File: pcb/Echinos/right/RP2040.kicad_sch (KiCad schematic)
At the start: 28 parts, among them SW224 Button, SW225 Button, SW226 Button, SW227 Button, U200 W25Q128JVP, U201 RP2040, Y200 Crystal_GND24

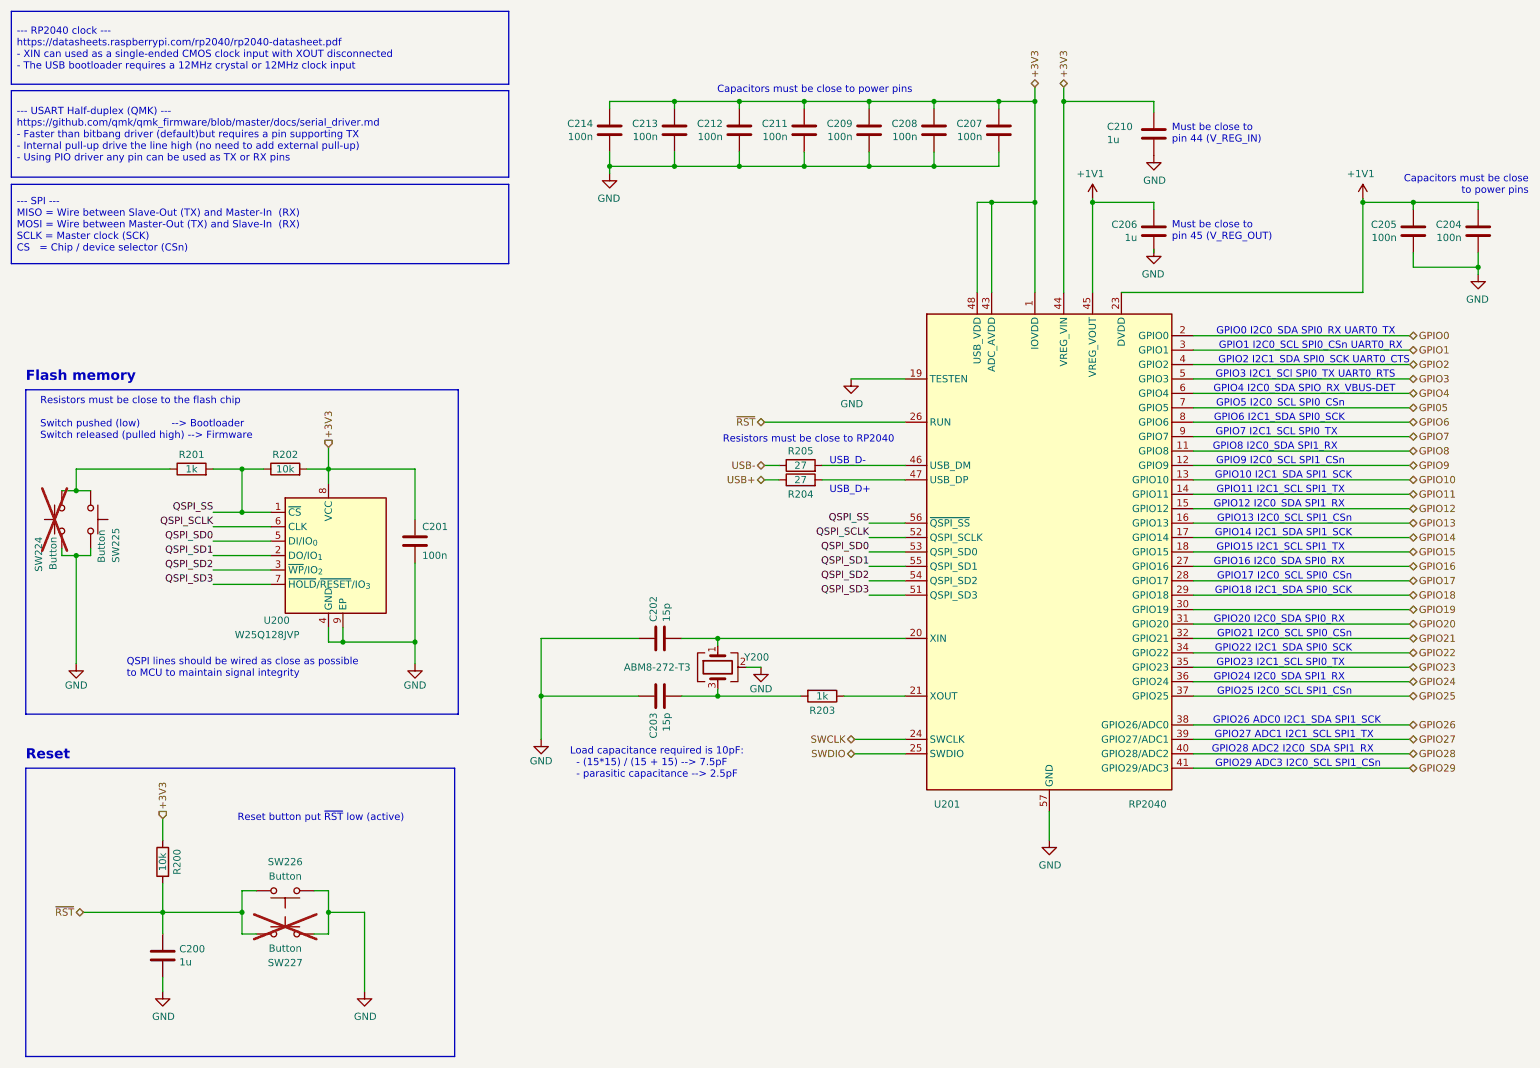
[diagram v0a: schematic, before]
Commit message: 💥 [PCB] - Group left and right on the same PCB.   - Schematics are different for each side   - Split trace naming to avoid mixing right and left   - Add mouse bite between both halves to make manufacturing easier (new footprint)
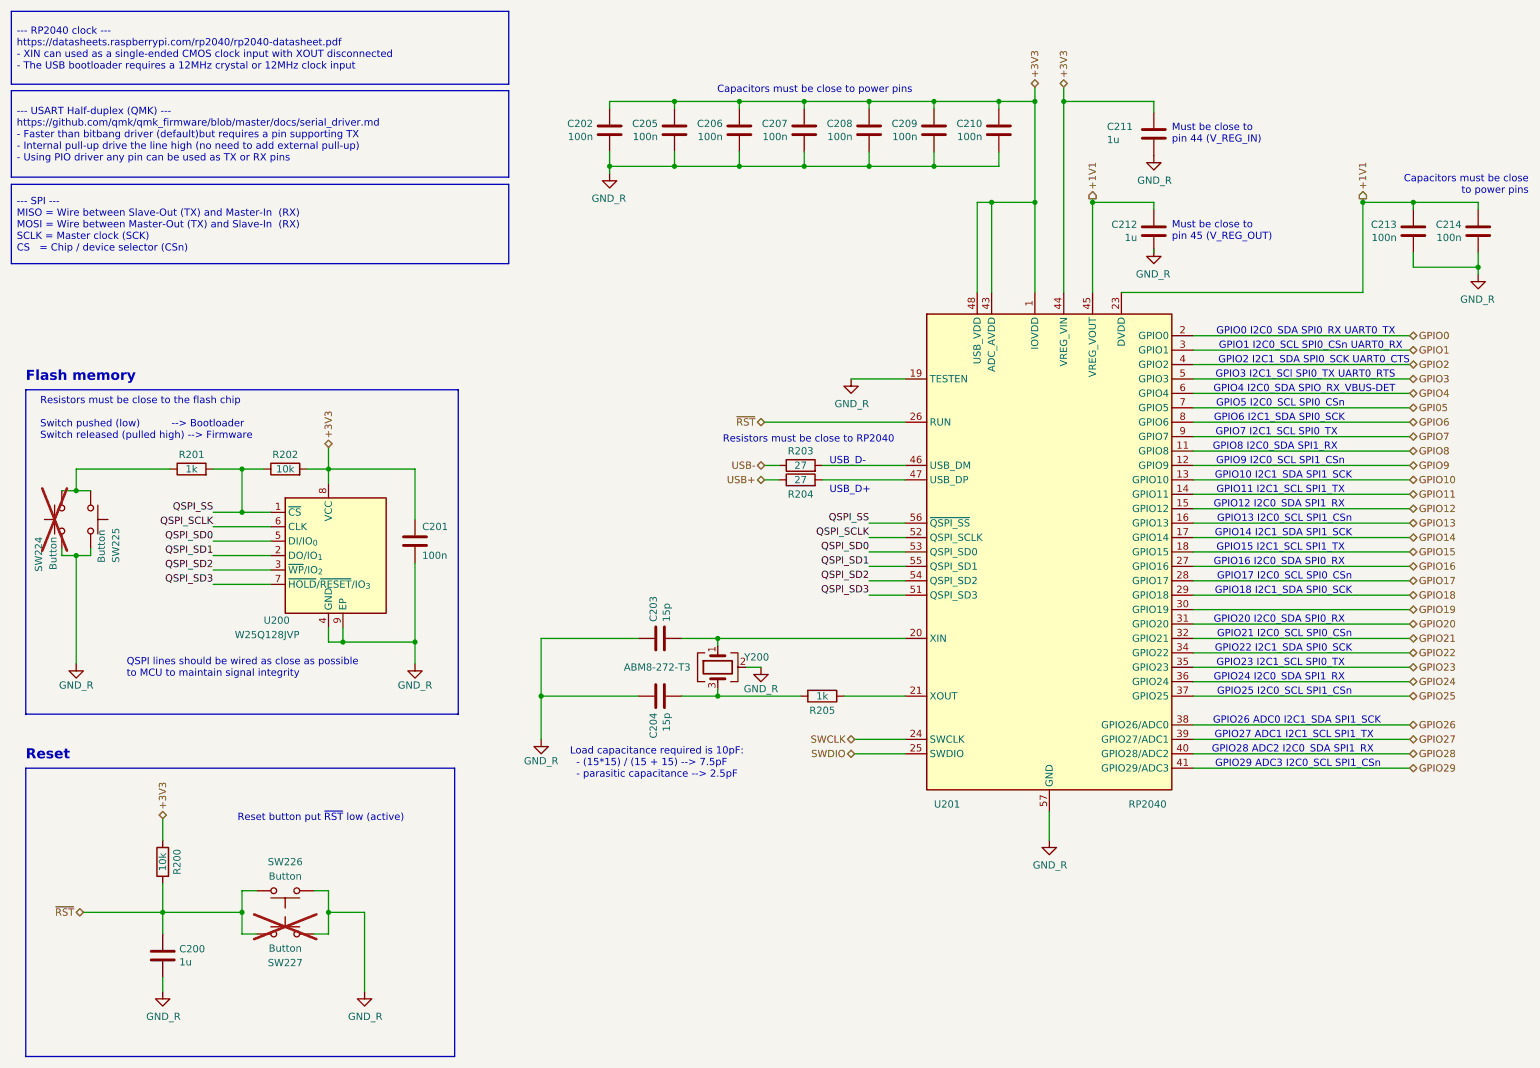
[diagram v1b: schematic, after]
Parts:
- C202: value 15p -> 100n; LCSC C86285 -> C1525; MFR CL05C150JB5NNNC -> CL05B104KO5NNNC
- C204: value 100n -> 15p; LCSC C1525 -> C86285; MFR CL05B104KO5NNNC -> CL05C150JB5NNNC
- C206, C210: value 1u -> 100n; LCSC C14445 -> C1525; MFR CL05A105KP5NNNC -> CL05B104KO5NNNC
- C211, C212: value 100n -> 1u; LCSC C1525 -> C14445; MFR CL05B104KO5NNNC -> CL05A105KP5NNNC
- R203: value 1k -> 27; LCSC C11702 -> C25100; MFR 0402WGF1001TCE -> 0402WGF270JTCE
- R205: value 27 -> 1k; LCSC C25100 -> C11702; MFR 0402WGF270JTCE -> 0402WGF1001TCE
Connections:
- net +1V1: now also C212.1, C213.1, C214.1; no longer C204.1, C205.1, C206.1
- net +3V3: now also C202.1, C205.1, C206.1; no longer C212.1, C213.1, C214.1
- net USB-: now also R203.1; no longer R205.1
- net at U201.20 (XIN), Y200.1: now also C203.2; no longer C202.2
- net at R205.2: now also C204.2, Y200.3; no longer U201.46 (USB_DM)
- net at U201.21 (XOUT): now also R205.1; no longer R203.1
- net GND renamed GND_R
- net GND_R: now also C202.2, C204.1; no longer C202.1, C204.2
- new net: R203.2, U201.46 (USB_DM)
